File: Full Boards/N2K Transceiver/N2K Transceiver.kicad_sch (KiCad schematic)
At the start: 76 parts, among them J1 Optional Bond, J2 PSU TP, J3 JTAG, SW1 SW_MEC_5G, SW2 SW_MEC_5G, SW3 SW_MEC_5G

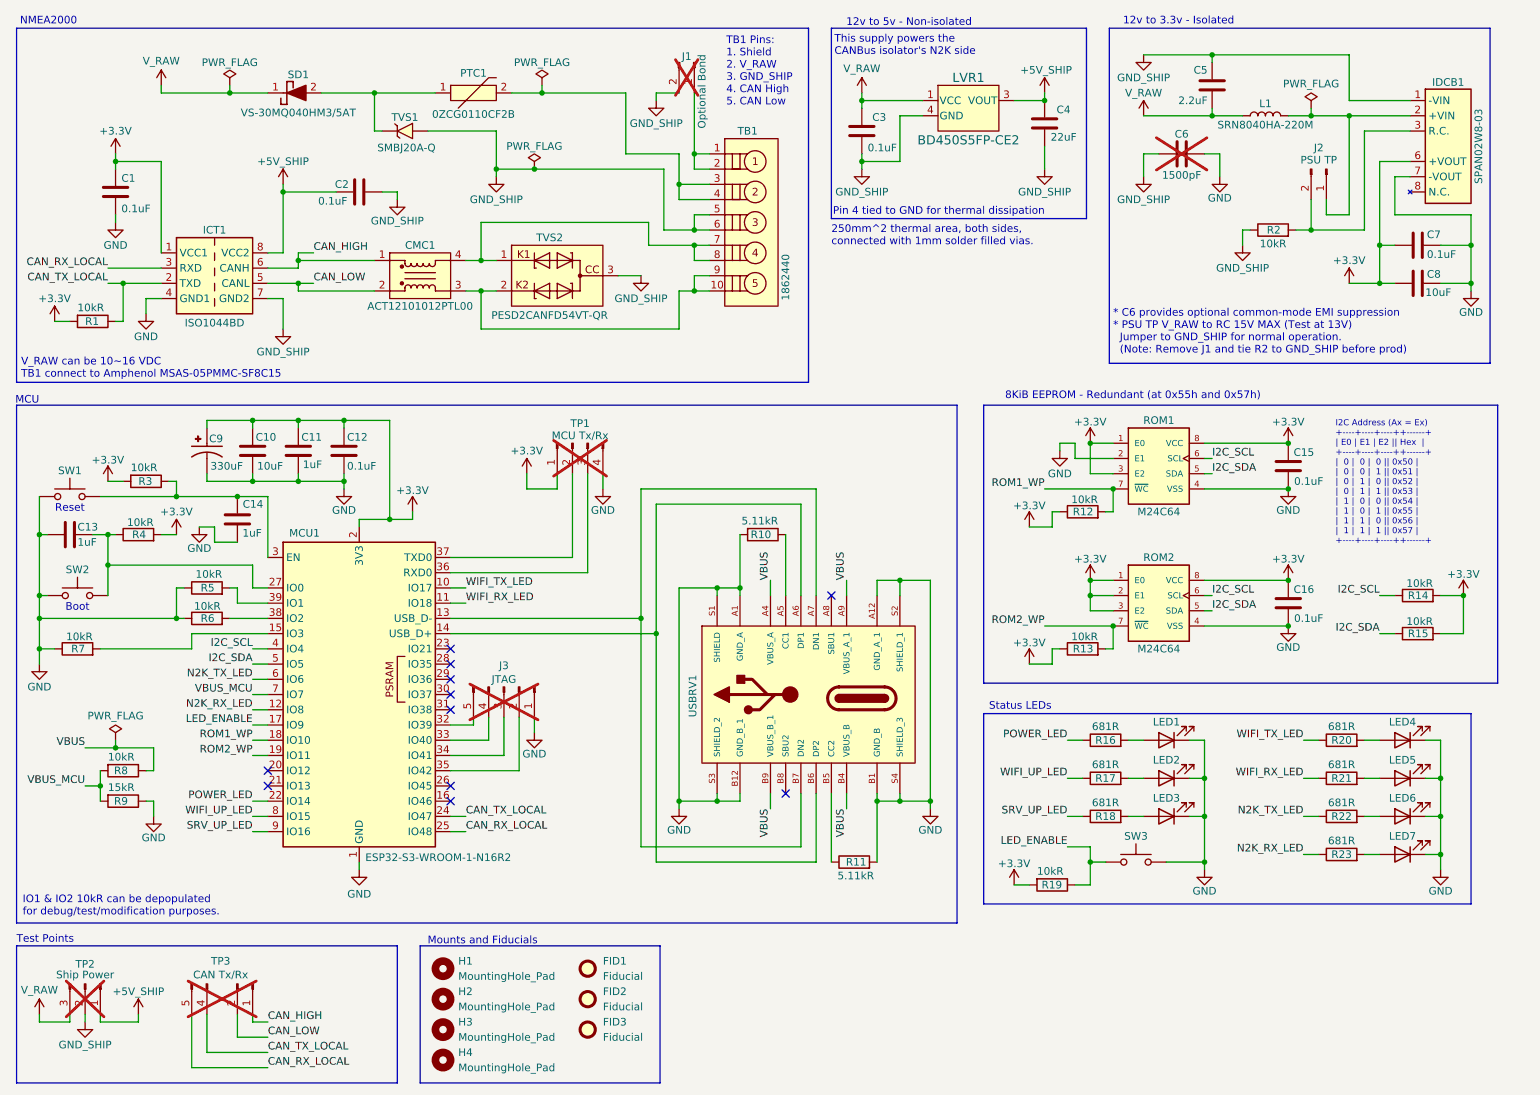
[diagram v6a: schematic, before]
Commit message: Refactoring to remove isolation. the real world benefits of isolation are weaker than the benefits of better energy efficiency. This also allows claiming LEN 1 on NMEA2000 instead of LEN 2.
Signed-off-by: digimer <digital.mermaid@gmail.com>
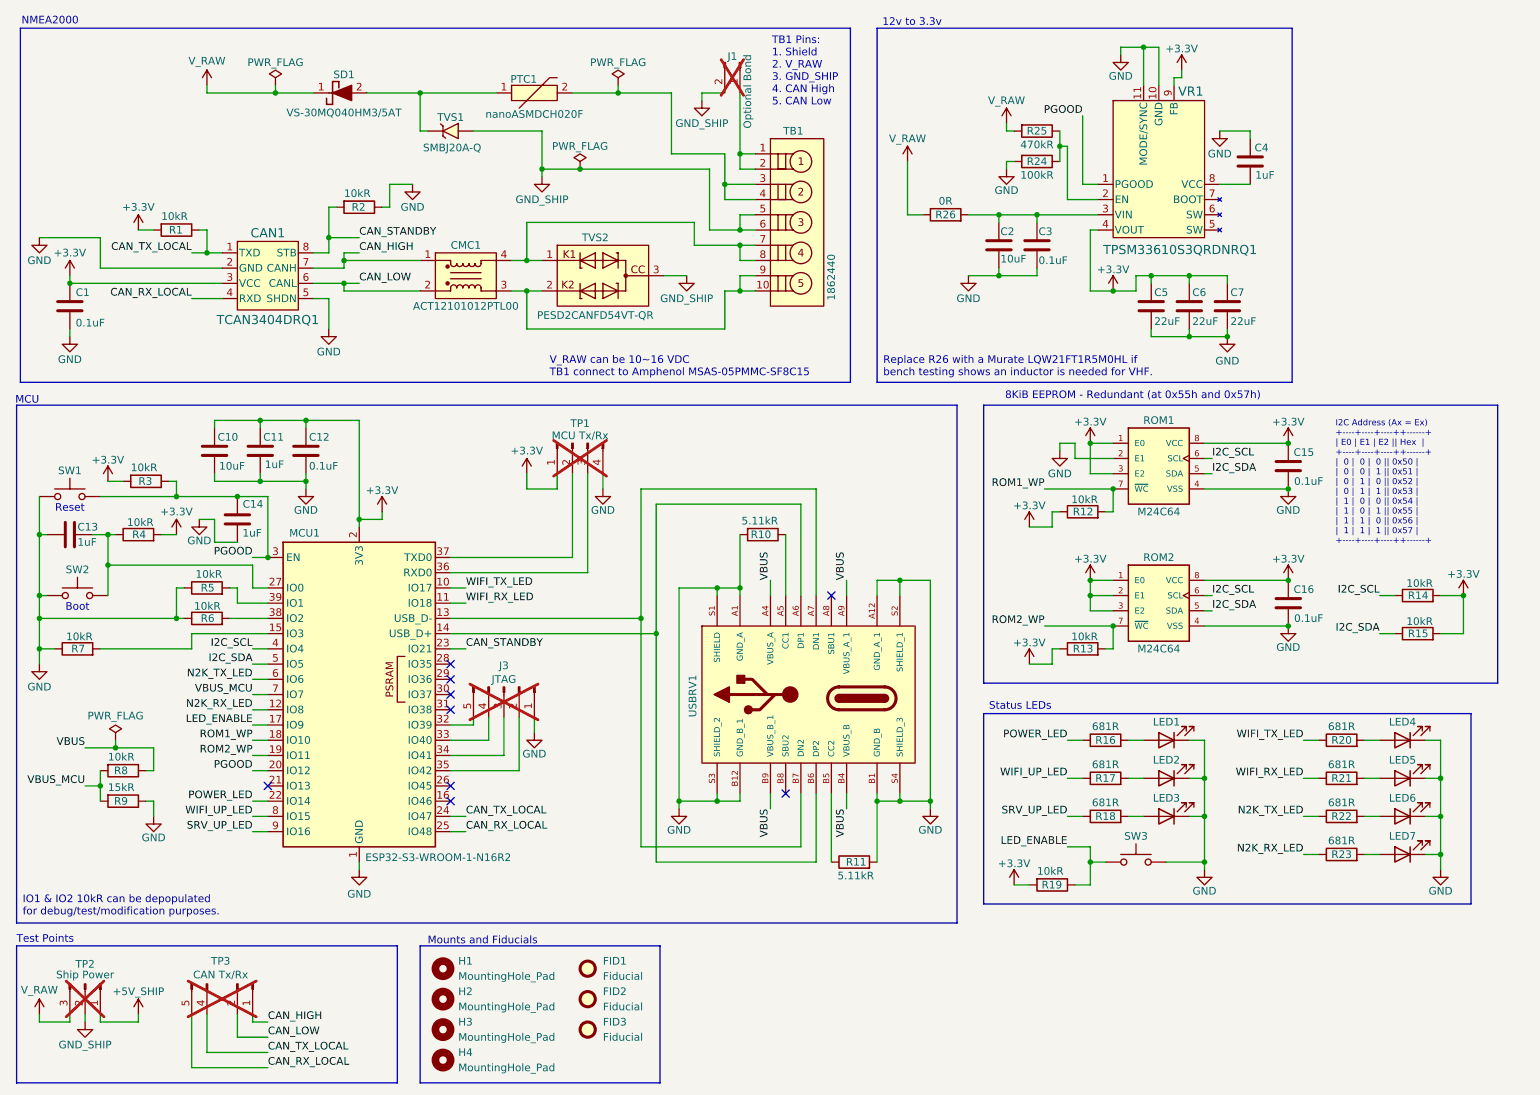
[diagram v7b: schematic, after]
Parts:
- removed C8: 10uF, mr-stuff:TDK CGA5, symbol Device:C
- removed C9: 330uF, mr-stuff:Panasonic EEH-ZU, symbol mr-parts:Panasonic EEH-ZU
- removed ICT1: ISO1044BD, mr-stuff:TI ISO1044BDR, symbol mr-parts:TI_ISO1044BDR
- removed IDCB1: SPAN02W8-03, mr-stuff:Mean Well SPAN02W8, symbol mr-parts:Mean Well SPAN02W8-03
- removed J2: PSU TP, Connector_PinHeader_2.54mm:PinHeader_1x02_P2.54mm_Vertical, symbol Connector:Conn_01x02_Pin
- removed L1: SRN8040HA-220M, mr-stuff:Bourns SRN8040HA, symbol Device:L
- removed LVR1: BD450S5FP-CE2, mr-stuff:Rohm BD4xxS5 TO252-3, symbol mr-parts:Rohm BD450S5FP-CE2
- added CAN1: TCAN3404DRQ1, mr-stuff:TI TCAN3404, symbol mr-parts:TI TCAN3404DRQ1
- added R24: 100kR, mr-stuff:Stackpole RMCA0805, symbol Device:R
- added R25: 470kR, mr-stuff:Wurth WRIS-RSKS, symbol Device:R
- added R26: 0R, mr-stuff:Vishay RCA-SR e3, symbol mr-parts:Vishay RCA08050000ZSEASR
- added VR1: TPSM33610S3QRDNRQ1, mr-stuff:TI TPSM336, symbol mr-parts:TI TPSM33606S3QRDNRQ1
- C2: value 0.1uF -> 10uF; footprint mr-stuff:Kyocera AVX 0805 -> mr-stuff:TDK CGA5; Part Kyocera 08051C104K4Z2A -> TDK CGA5L1X7R1H106K160AE
- C4: value 22uF -> 1uF; footprint mr-stuff:Murata GCJ31CR71A -> mr-stuff:Kyocera AVX 0805; Part Murata GCJ31CR71A226KE01L -> Kyocera 08051C105K4Z2A
- C5: value 2.2uF -> 22uF; footprint mr-stuff:Kyocera AVX 1210 -> mr-stuff:Murata GCJ32ER71C; Part Kyocera AVX 12101C225K4Z2A -> Murata GCJ32ER71C226KE01L
- C6: value 1500pF -> 22uF; footprint mr-stuff:Knowles Syfer 1808YA25 -> mr-stuff:Murata GCJ32ER71C; Part Knowles Syfer 1808YA250152KSTSYX -> Murata GCJ32ER71C226KE01L; now fitted; now in the parts list
- C7: value 0.1uF -> 22uF; footprint mr-stuff:Kyocera AVX 0805 -> mr-stuff:Murata GCJ32ER71C; Part Kyocera 08051C104K4Z2A -> Murata GCJ32ER71C226KE01L
- PTC1: value 0ZCG0110CF2B -> nanoASMDCH020F; footprint mr-stuff:Bel Fuse 0ZCG -> mr-stuff:Littelfuse NANOASMDCH020F; symbol mr-parts:Bel Fuse 0ZCG0110CF2B -> mr-parts:Littelfuse nanoASMDCH020F; Part Bel Fuse 0ZCG0110CF2B -> Littelfuse nanoASMDCH020F
- SD1: Height Vishay VS-30MQ040-M3_5AT -> (none); Part (none) -> Vishay VS-30MQ040-M3_5AT
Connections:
- net +3.3V: now also C5.1, C6.1, CAN1.3 (VCC), VR1.4 (VOUT), VR1.9 (FB)
- net +5V_SHIP: no longer C2.2, C4.2
- net CAN_HIGH: now also CAN1.7 (CANH)
- net CAN_LOW: now also CAN1.6 (CANL)
- net CAN_RX_LOCAL: now also CAN1.4 (RXD)
- net CAN_TX_LOCAL: now also CAN1.1 (TXD)
- net GND: now also C2.2, C3.2, C4.2, C5.2, C6.2, R2.1, CAN1.2 (GND), CAN1.5 (SHDN), R24.2, VR1.10 (GND), VR1.11 (MODE/SYNC); no longer C6.1
- net GND_SHIP: no longer C2.1, C3.1, C4.1, C5.2, C6.2, R2.1
- net V_RAW: now also R25.2, R26.1; no longer C3.2, C5.1
- net PGOOD: now reaches C14.2, MCU1.3 (EN), R3.1, SW1.3 (B), SW1.4 (B)
- net PGOOD: now also MCU1.20 (IO12), VR1.1 (PGOOD)
- net CAN_STANDBY: now reaches R2.2
- net CAN_STANDBY: now also MCU1.23 (IO21), CAN1.8 (STB)
- new net: C2.1, C3.1, R26.2, VR1.3 (VIN)
- new net: R24.1, R25.1, VR1.2 (EN)
- new net: C4.1, VR1.8 (VCC)
- no-connect marks 11 -> 9
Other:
- note added: "12v to 3.3v"
- note added: "Replace R26 with a Murate LQW21FT1R5M0HL if bench testing shows an inductor is needed for VHF."
- note removed: "* C6 provides optional common-mode EMI suppression * PSU TP V_RAW to RC 15V MAX (Test at 13V) Jumper to GND_SHIP for normal operation. (Note: Remove J1 and tie R2 to GND_SHIP before prod)"
- note removed: "12v to 3.3v - Isolated"
- note removed: "12v to 5v - Non-isolated"
- note removed: "250mm^2 thermal area, both sides, connected with 1mm solder filled vias."
- note removed: "Pin 4 tied to GND for thermal dissipation"
- note removed: "This supply powers the CANBus isolator's N2K side"
- moved on the sheet: C1, C10, C11, C12, CMC1, J1, PTC1, R1, SD1, TB1, TVS1, TVS2

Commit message: Updated the capacitors and added an input resistor to MCU_RESET (formerly PGOOD net).
Signed-off-by: digimer <digital.mermaid@gmail.com>
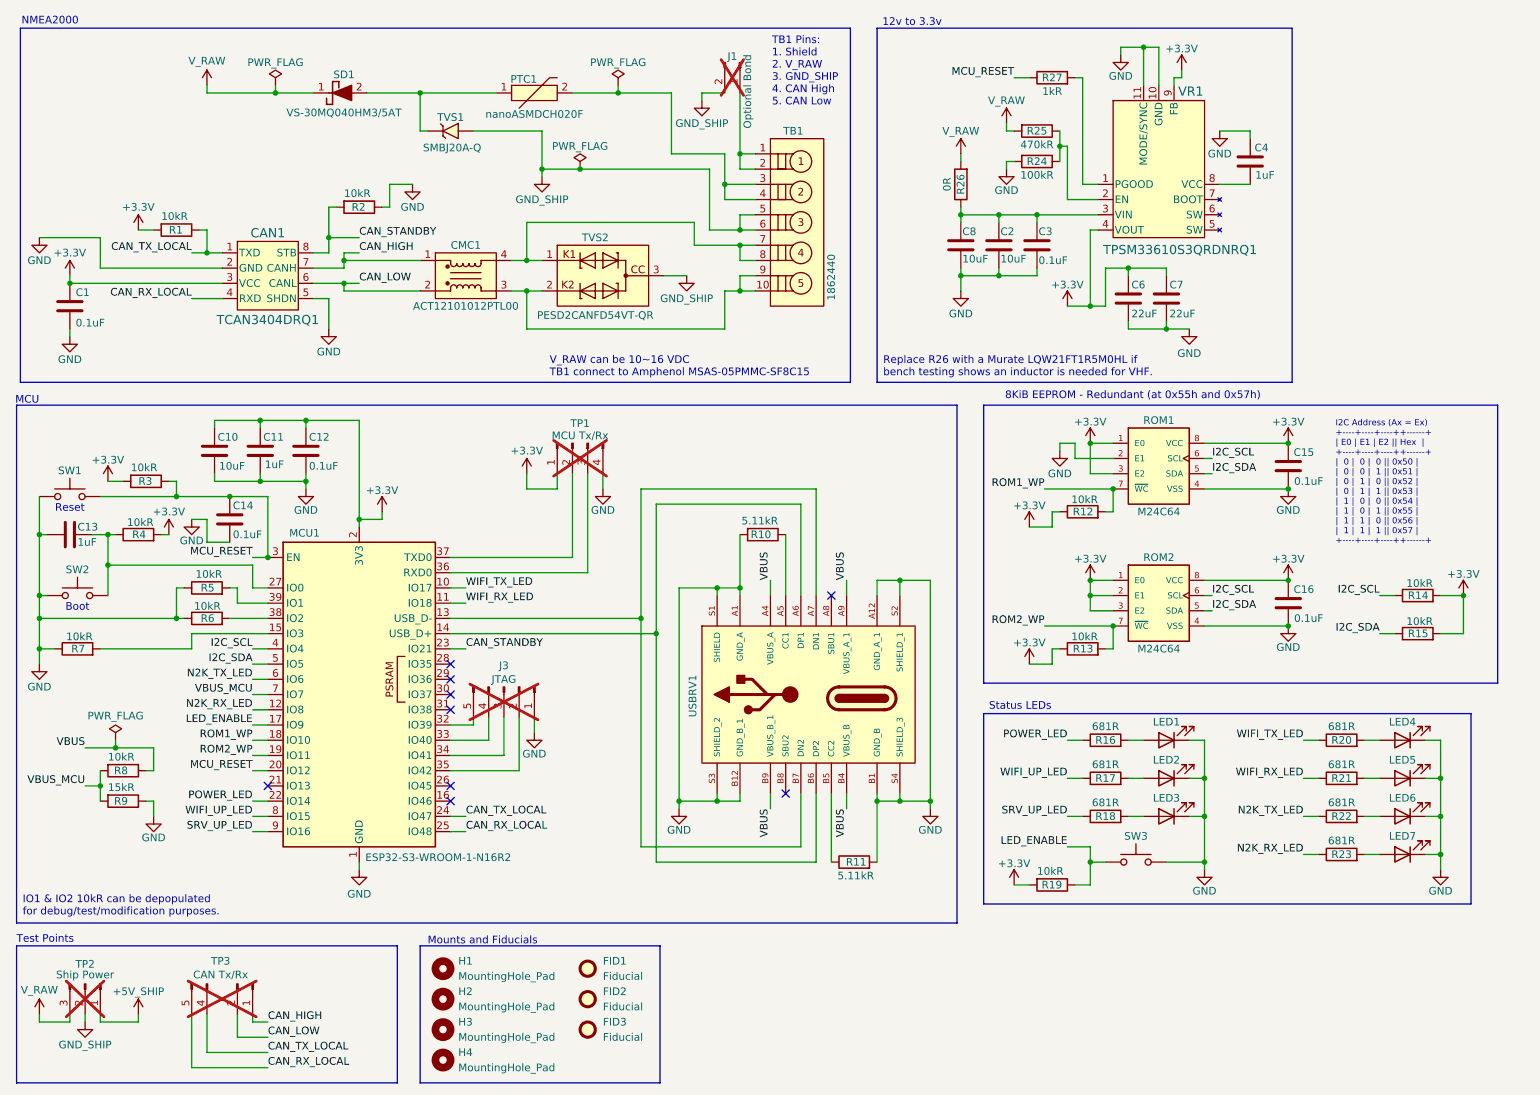
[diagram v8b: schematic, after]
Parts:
- removed C5: 22uF, mr-stuff:Murata GCJ32ER71C, symbol Device:C
- added C8: 10uF, mr-stuff:TDK CGA5, symbol Device:C
- added R27: 1kR, mr-stuff:Stackpole RNCP0805, symbol mr-parts:Stackpole RNCP0805FTD1K00
- C14: value 1uF -> 0.1uF; Part Kyocera 08051C105K4Z2A -> Kyocera 08051C104K4Z2A
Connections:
- net GND: now also C14.2, C8.2; no longer C14.1
- net V_RAW: now also R26.2; no longer R26.1
- net at C2.1, C3.1, VR1.3 (VIN): now also R26.1, C8.1; no longer R26.2
- net PGOOD renamed MCU_RESET
- net MCU_RESET: now also C14.1, R27.1; no longer C14.2, VR1.1 (PGOOD)
- new net: R27.2, VR1.1 (PGOOD)
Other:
- moved on the sheet: C6, C7, R26
